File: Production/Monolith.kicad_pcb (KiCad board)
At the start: 6 copper layers, 45.5 x 45.5 mm, 246 parts, among them J102 Cell 1 NTC wires, J105 Cell 2 NTC wires, J106 Cell 3 NTC wires, J107 Cell 4 NTC wires, J108 PACK- (CELL_N), J109 CELL1 tap, J110 CELL2 tap, J111 CELL3 tap, J112 PACK+ (CELL_P_RAW), J301 TC2030-NL, J401 TYPE-C 16PCB0.8 IP68, J501 TYPE-C 16PCB0.8 IP68, Q101 AGM404AP1, Q102 AGM404AP1, Q103 AO3400A, Q104 AO3400A, Q401 SiZ240DT, Q402 SiZ240DT, Q501 SiZ240DT, Q502 SiZ240DT, U101 BQ40Z50RSMR-R2, U102 BQ294700DSGR, U204 TPS62177DQCR, U301 CC2340R5MODA, U401 TPS25751DREFR, U402 M24512-DFMC6TG, U403 BQ25756RRVR, U404 TPS62933DRLR, U405 TPD2S300YFFR, U501 TPS25751DREFR, U502 M24512-DFMC6TG, U503 BQ25756RRVR, U504 TPS62933DRLR, U505 TPD2S300YFFR

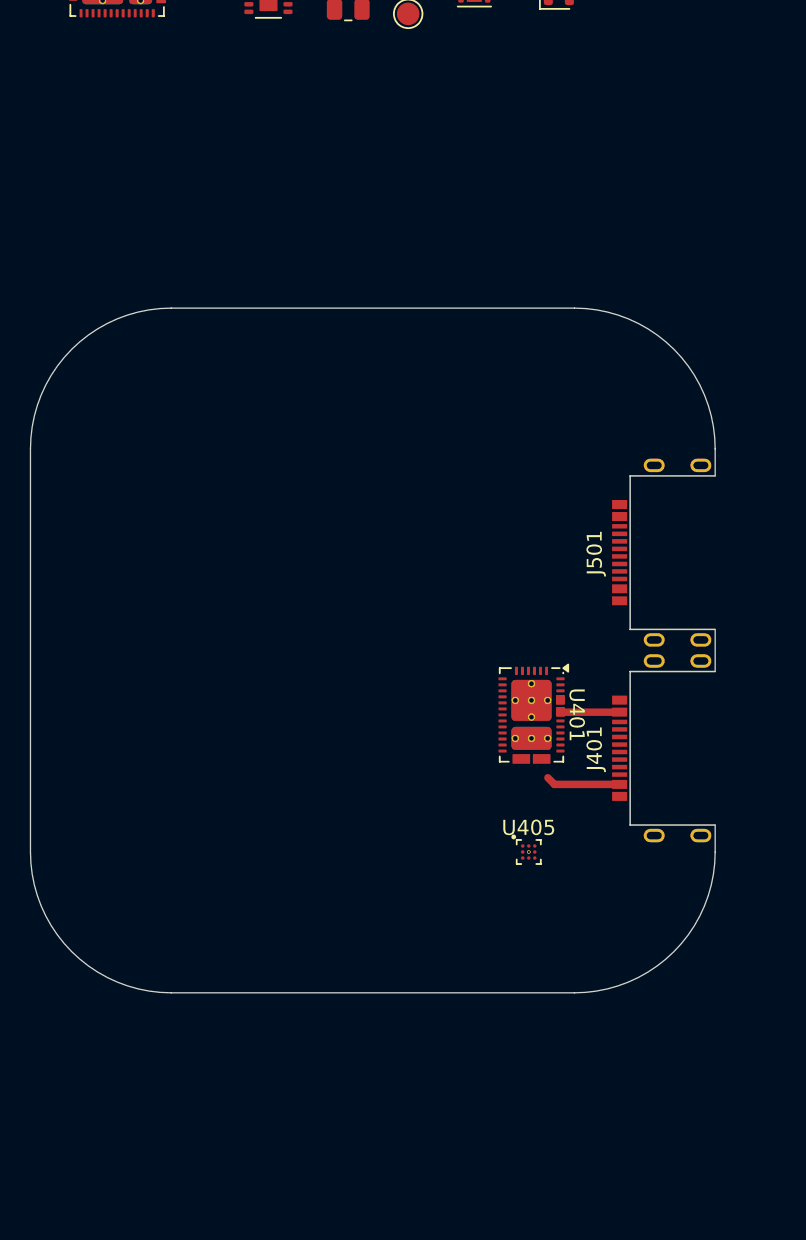
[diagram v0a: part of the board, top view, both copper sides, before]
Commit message: Production board: side outline and 1.6 mm thickness (for cost)
- Monolith.kicad_pcb: 43.2 x 74.35 mm side-board outline with bottom
  corners notched around the tray's screw pillars; J501/J401 on the top
  edge at x 93.5 / 106.5, 180 deg, locked. Stack-up 6 layers 1.6 mm
  (symmetric approximation; use JLC's stack at order time).
- make_board.py imports the outline from mechanical/monolith_shell.py
  (one source for tray and board). New --keep-copper flag: the four
  hand-drawn VBUS traces near the old J401 position are kept as they
  were and now dangle.
- J401/J501: TYPE-C 16PCB1.6 IP68 (C55629729) in the schematic, board
  and make_production.py; same land pattern as the 0.8 mm part.
- mechanical: SB_PCB_T = 1.6, USB-C centreline derived from it; the
  pack is 0.8 mm wider (55.2 x 49.0 x 83.0 with bumpers, ~338 g). All
  assembly checks pass; STLs and render regenerated.
- Docs: Production README (stack-up, JLC via limits at 1.6 mm, new
  side-outline section, history notes), root README, next-actions log.

DRC: no outline errors; remaining items are the known pending schematic
update, the TPD2S300 via-in-pad and the 3 dangling VBUS traces.

Co-Authored-By: Claude Opus 5.5 <noreply@anthropic.com>
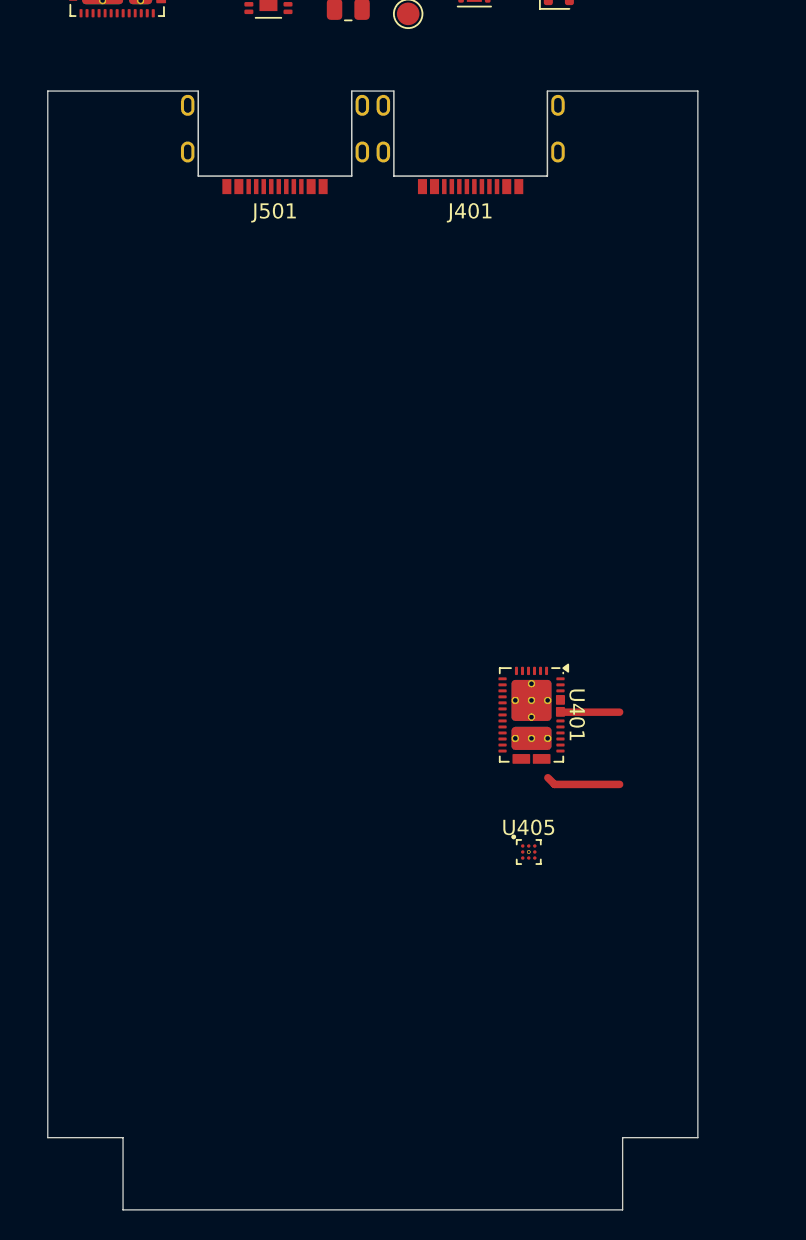
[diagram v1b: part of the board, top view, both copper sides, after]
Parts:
- J401, J501: value TYPE-C 16PCB0.8 IP68 -> TYPE-C 16PCB1.6 IP68; footprint MonolithDev:USB_C_Receptacle_ShouHan_TYPE-C_16PCB0.8_IP68 -> MonolithDev:USB_C_Receptacle_ShouHan_TYPE-C_16PCB1.6_IP68
- moved J401 46.6 mm to (106.5, 62.8), turned to 180 degrees
- moved J501 42.4 mm to (93.5, 62.8), turned to 180 degrees
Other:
- board size 45.5 x 45.5 mm -> 43.2 x 74.4 mm

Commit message: Production: U405/U505 TPD2S300 -> TPD6S300 (no via-in-pad)
The TPD2S300's WCSP-9 centre ball needed a 0.15 mm via-in-pad, below
JLC's no-surcharge hole size and the project's 0.3 mm drill rule. The
TPD6S300RUKR (WQFN-20 3x3, LCSC C2649810) does the same CC job
(24 V short-to-VBUS OVP, IEC ESD, FLT) and fans out with standard vias.

- tools/tpd6s300.py: symbol, pin nets, and a footprint from KiCad's
  RUK0020B with four 0.3/0.5 mm vias in the exposed pad
- RPD_G1/G2 -> C_CC1/C_CC2 for dead-battery Rd; SBU and D1/D2 unused
- board: footprints swapped in place, U405 moved 0.65 mm clear of U401
- IVPWR is 90 uA typ per part (TPD2S300: 3.2 uA), noted in the README

Co-Authored-By: Claude Opus 5.5 <noreply@anthropic.com>
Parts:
- U405, U505: value TPD2S300YFFR -> TPD6S300RUKR; footprint MonolithDev:TI_YFF0009_DSBGA-9_P0.4mm -> MonolithDev:TI_RUK0020B_WQFN-20-1EP_3x3mm_P0.4mm_EP1.7x1.7mm_Via0.3
- moved U405 0.65 mm to (110.4, 114.0)

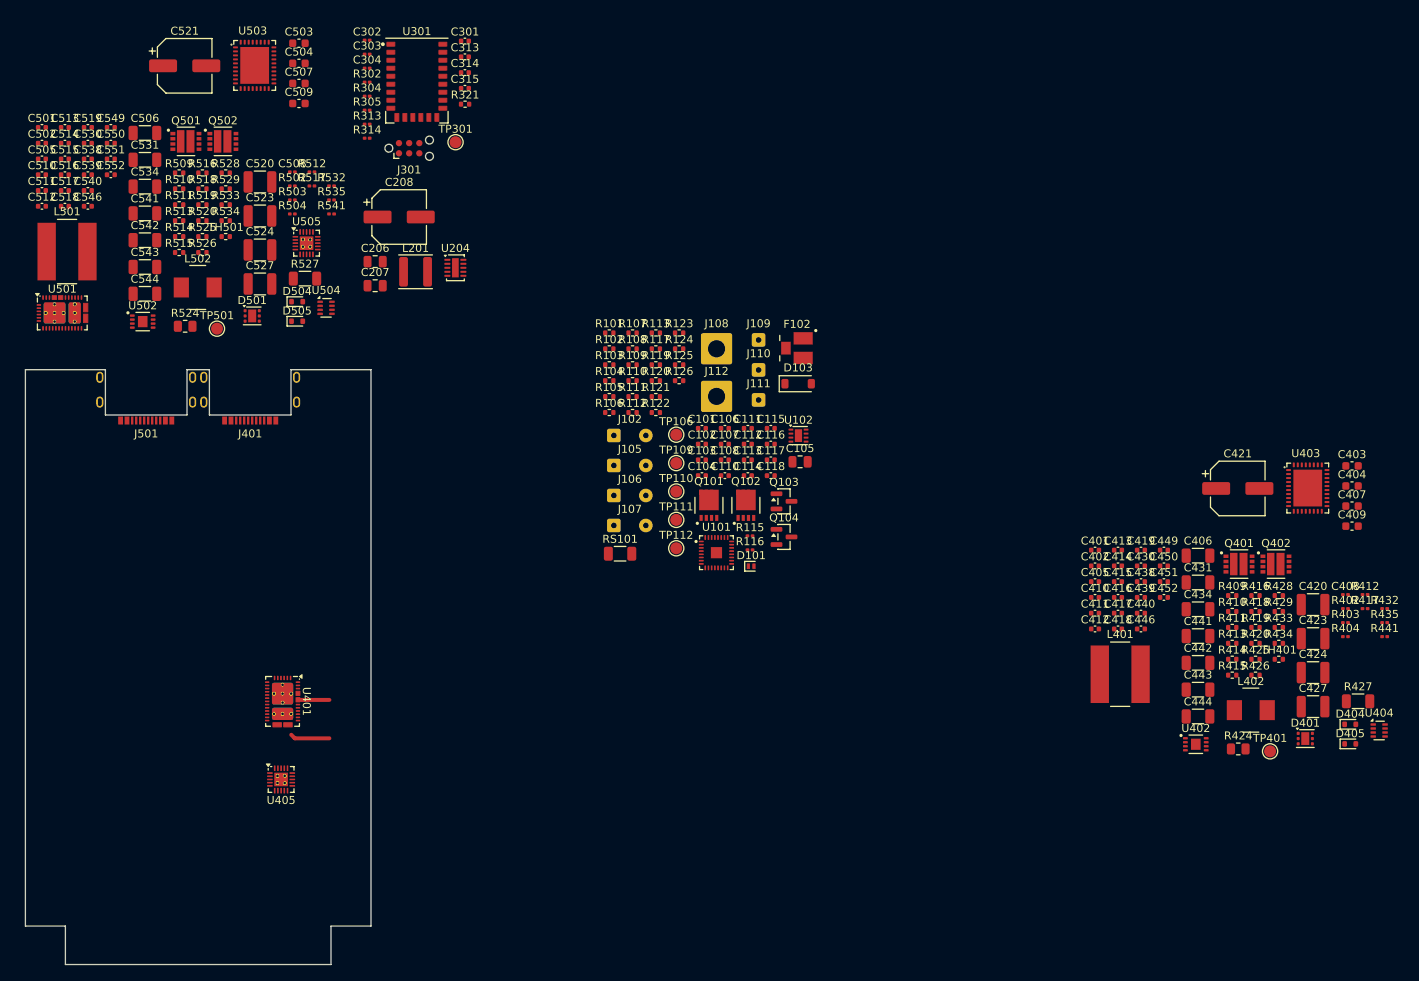
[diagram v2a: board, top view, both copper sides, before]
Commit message: Production board layout in progress; CCS debug target and settings; cover marking zip
Commits the working tree as it stood: Production/Monolith.kicad_pcb and
.kicad_pro (layout work), firmware/targets/CC2340R53 (1).ccxml and
firmware/.theia/settings.json (CCS), mechanical/monolith_side_cover_marking.zip,
and removes a stale LibreOffice lock file under DevBoard/fab.

Co-Authored-By: Claude Opus 5.5 <noreply@anthropic.com>
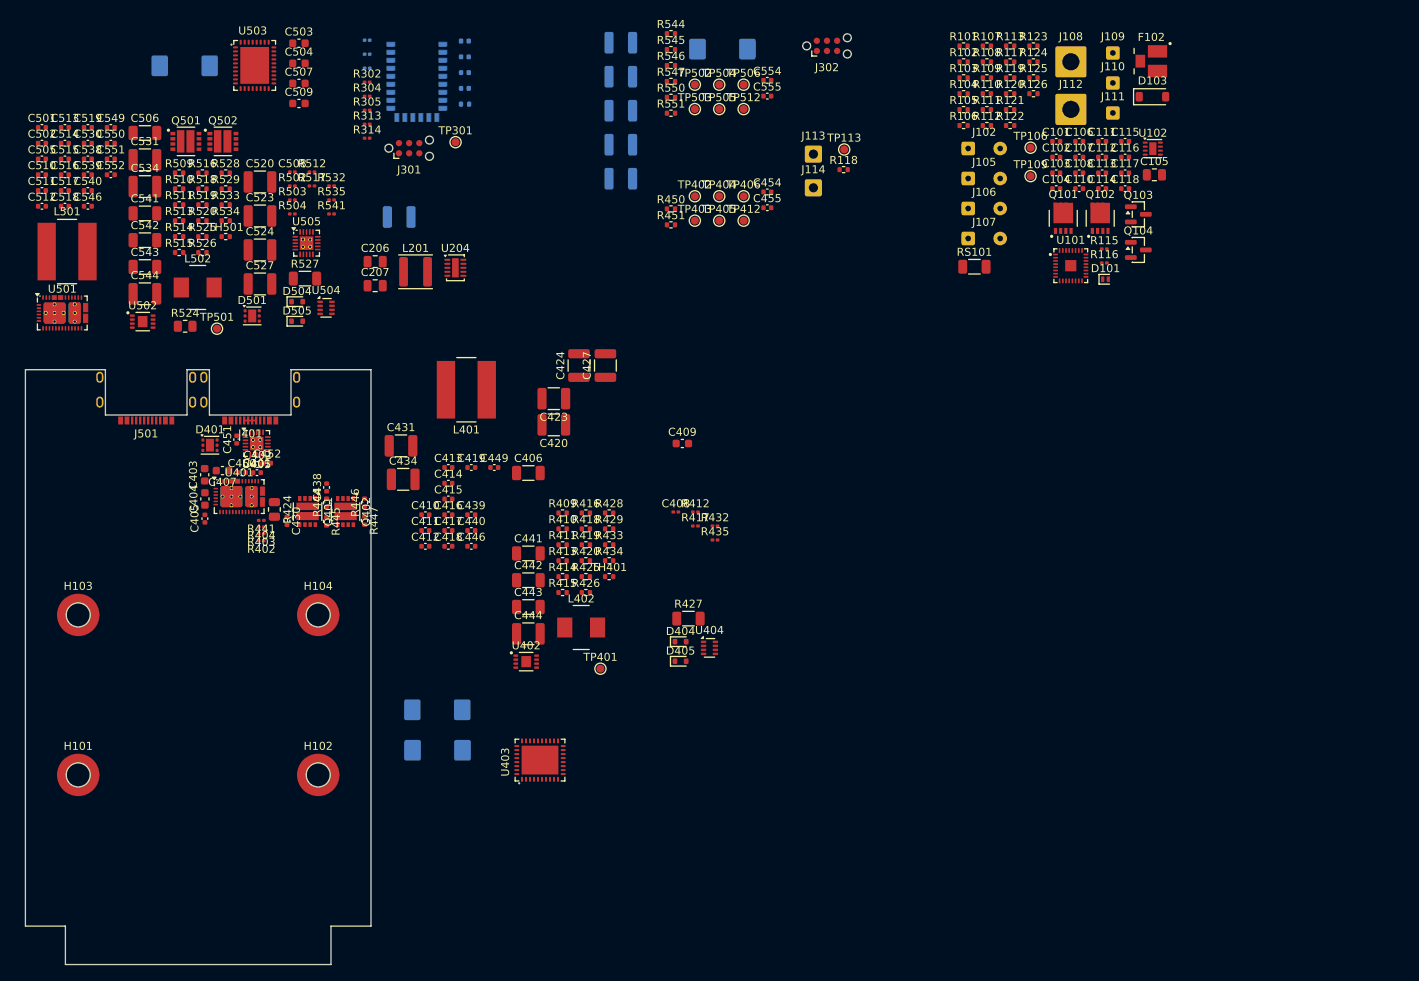
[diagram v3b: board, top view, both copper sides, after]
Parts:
- removed TP110: SMBC, TestPoint:TestPoint_Pad_D1.5mm
- removed TP111: SMBD, TestPoint:TestPoint_Pad_D1.5mm
- removed TP112: GND, TestPoint:TestPoint_Pad_D1.5mm
- added C209: 22u 35V, Capacitor_SMD:C_1210_3225Metric, B.Cu at (152.8, 21.9)
- added C210: 22u 35V, Capacitor_SMD:C_1210_3225Metric, B.Cu at (152.8, 26.2)
- added C211: 22u 35V, Capacitor_SMD:C_1210_3225Metric, B.Cu at (152.8, 30.4)
- added C212: 22u 35V, Capacitor_SMD:C_1210_3225Metric, B.Cu at (152.8, 34.7)
- added C213: 22u 35V, Capacitor_SMD:C_1210_3225Metric, B.Cu at (152.8, 38.9)
- added C454: 33p C0G, Capacitor_SMD:C_0402_1005Metric, F.Cu at (171.1, 40.6)
- added C455: 33p C0G, Capacitor_SMD:C_0402_1005Metric, F.Cu at (171.1, 42.6)
- added C456: 47u 35V, Capacitor_Tantalum_SMD:CP_EIA-7343-31_Kemet-D, B.Cu at (129.9, 110.4)
- added C554: 33p C0G, Capacitor_SMD:C_0402_1005Metric, F.Cu at (171.1, 26.7)
- added C555: 33p C0G, Capacitor_SMD:C_0402_1005Metric, F.Cu at (171.1, 28.6)
- added C556: 47u 35V, Capacitor_Tantalum_SMD:CP_EIA-7343-31_Kemet-D, B.Cu at (165.5, 22.7)
- added H101: WA-SMSI M2 3.5mm, Mounting_Wuerth:Mounting_Wuerth_WA-SMSI-M2_H3.5mm_9774035243, F.Cu at (85.0, 113.5)
- added H102: WA-SMSI M2 3.5mm, Mounting_Wuerth:Mounting_Wuerth_WA-SMSI-M2_H3.5mm_9774035243, F.Cu at (115.0, 113.5)
- added H103: WA-SMSI M2 3.5mm, Mounting_Wuerth:Mounting_Wuerth_WA-SMSI-M2_H3.5mm_9774035243, F.Cu at (85.0, 93.5)
- added H104: WA-SMSI M2 3.5mm, Mounting_Wuerth:Mounting_Wuerth_WA-SMSI-M2_H3.5mm_9774035243, F.Cu at (115.0, 93.5)
- added J113: LOAD PACK_P, Connector_Wire:SolderWire-0.5sqmm_1x01_D0.9mm_OD2.1mm, F.Cu at (176.9, 35.9)
- added J114: LOAD GND, Connector_Wire:SolderWire-0.5sqmm_1x01_D0.9mm_OD2.1mm, F.Cu at (176.9, 40.1)
- added J302: TC2030-NL GAUGE, Connector:Tag-Connect_TC2030-IDC-NL_2x03_P1.27mm_Vertical, F.Cu at (178.6, 22.3)
- added R118: 4.7k, Resistor_SMD:R_0402_1005Metric, F.Cu at (180.7, 37.8)
- added R444: 0R, Resistor_SMD:R_0402_1005Metric, F.Cu at (116.0, 79.4)
- added R445: 0R, Resistor_SMD:R_0402_1005Metric, F.Cu at (116.0, 81.8)
- added R446: 0R, Resistor_SMD:R_0402_1005Metric, F.Cu at (120.8, 79.4)
- added R447: 0R, Resistor_SMD:R_0402_1005Metric, F.Cu at (120.8, 81.7)
- added R450: 3R3, Resistor_SMD:R_0402_1005Metric, F.Cu at (159.1, 42.7)
- added R451: 3R3, Resistor_SMD:R_0402_1005Metric, F.Cu at (159.1, 44.7)
- added R544: 0R, Resistor_SMD:R_0402_1005Metric, F.Cu at (159.1, 20.8)
- added R545: 0R, Resistor_SMD:R_0402_1005Metric, F.Cu at (159.1, 22.8)
- added R546: 0R, Resistor_SMD:R_0402_1005Metric, F.Cu at (159.1, 24.8)
- added R547: 0R, Resistor_SMD:R_0402_1005Metric, F.Cu at (159.1, 26.8)
- added R550: 3R3, Resistor_SMD:R_0402_1005Metric, F.Cu at (159.1, 28.8)
- added R551: 3R3, Resistor_SMD:R_0402_1005Metric, F.Cu at (159.1, 30.8)
- added TP113: WAKE, TestPoint:TestPoint_Pad_D1.0mm, F.Cu at (180.8, 35.3)
- added TP402: PPHV, TestPoint:TestPoint_Pad_D1.0mm, F.Cu at (162.1, 41.1)
- added TP403: PP5V, TestPoint:TestPoint_Pad_D1.0mm, F.Cu at (162.1, 44.2)
- added TP404: REGN, TestPoint:TestPoint_Pad_D1.0mm, F.Cu at (165.1, 41.1)
- added TP405: SW1, TestPoint:TestPoint_Pad_D1.0mm, F.Cu at (165.1, 44.2)
- added TP406: SW2, TestPoint:TestPoint_Pad_D1.0mm, F.Cu at (168.2, 41.1)
- added TP412: GND, TestPoint:TestPoint_Pad_D1.0mm, F.Cu at (168.2, 44.2)
- added TP502: PPHV, TestPoint:TestPoint_Pad_D1.0mm, F.Cu at (162.1, 27.2)
- added TP503: PP5V, TestPoint:TestPoint_Pad_D1.0mm, F.Cu at (162.1, 30.2)
- added TP504: REGN, TestPoint:TestPoint_Pad_D1.0mm, F.Cu at (165.1, 27.2)
- added TP505: SW1, TestPoint:TestPoint_Pad_D1.0mm, F.Cu at (165.1, 30.2)
- added TP506: SW2, TestPoint:TestPoint_Pad_D1.0mm, F.Cu at (168.2, 27.2)
- added TP512: GND, TestPoint:TestPoint_Pad_D1.0mm, F.Cu at (168.2, 30.2)
- C208: value 100u 25V -> 22u 35V; footprint Capacitor_SMD:CP_Elec_6.3x7.7 -> Capacitor_SMD:C_1210_3225Metric; moved to B.Cu
- C301, C302, C303, C304, C313, C314, C315, R321, U301: moved to B.Cu
- C421, C521: value 100u 35V -> 47u 35V; footprint Capacitor_SMD:CP_Elec_6.3x7.7 -> Capacitor_Tantalum_SMD:CP_EIA-7343-31_Kemet-D; moved to B.Cu
- C431, C434, C531, C534: value 22u 25V -> 22u 35V; footprint Capacitor_SMD:C_1206_3216Metric -> Capacitor_SMD:C_1210_3225Metric
- C444, C544: value 10u 50V -> 22u 35V; footprint Capacitor_SMD:C_1206_3216Metric -> Capacitor_SMD:C_1210_3225Metric
- J108: value PACK- (CELL_N) -> PACK-
- J112: value PACK+ (CELL_P_RAW) -> PACK+
- R424, R524: value 5m 0.5W (RAC) -> 5m 0.5W
- TP106, TP109, TP301, TP401, TP501: footprint TestPoint:TestPoint_Pad_D1.5mm -> TestPoint:TestPoint_Pad_D1.0mm
- moved C403 143.4 mm to (100.8, 76.0), turned to 90 degrees
- moved C404 143.4 mm to (100.8, 79.0), turned to -90 degrees
- moved D401 141.7 mm to (101.5, 72.3)
- moved C407 141.3 mm to (103.0, 75.4), turned to 180 degrees
- moved R441 141.2 mm to (107.9, 81.7), turned to 180 degrees
- moved R404 136.2 mm to (107.9, 82.5), turned to 180 degrees
- moved R403 136.0 mm to (107.9, 83.3), turned to 180 degrees
- moved R402 135.8 mm to (107.9, 84.2), turned to 180 degrees
- moved R424 124.1 mm to (109.5, 80.3), turned to -90 degrees
- moved C451 117.3 mm to (104.8, 71.6), turned to 90 degrees
- moved Q401 116.6 mm to (113.7, 80.6), turned to -90 degrees
- moved Q402 116.5 mm to (118.4, 80.6), turned to -90 degrees
- moved C450 115.8 mm to (105.5, 75.7)
- moved C452 113.4 mm to (108.6, 74.5)
- moved C405 111.5 mm to (100.8, 81.4), turned to -90 degrees
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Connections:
- Q401 pad 1: /USB Port 1/HIDRV1 -> /USB Port 1/HG1
- Q401 pad 8: /USB Port 1/LODRV1 -> /USB Port 1/LG1
- Q402 pad 1: /USB Port 1/HIDRV2 -> /USB Port 1/HG2
- Q402 pad 8: /USB Port 1/LODRV2 -> /USB Port 1/LG2
- Q501 pad 1: /USB Port 2/HIDRV1 -> /USB Port 2/HG1
- Q501 pad 8: /USB Port 2/LODRV1 -> /USB Port 2/LG1
- Q502 pad 1: /USB Port 2/HIDRV2 -> /USB Port 2/HG2
- Q502 pad 8: /USB Port 2/LODRV2 -> /USB Port 2/LG2
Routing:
- net /USB Port 1/VBUS: track 8.89 -> 0.00 mm
- net /USB Port 1/DPDN_DCP: track 0.00 -> 1.50 mm
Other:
- board text added: "KO_NOTE B.Cu (faces the cells, hand-soldered): parts <= 2.3 mm tall; up to ~5 mm only in the centre strip x 96-104 or beyond 18 mm from centre. No heat sources on B.Cu. F.Cu: parts <= 3.2 mm (cover gap pad)."
